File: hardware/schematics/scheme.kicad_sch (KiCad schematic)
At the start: 10 parts

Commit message: changed schema
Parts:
- added CD1: Data Connector, symbol Connector:Conn_01x02_Pin
- added CW1: Power Connector, symbol Connector:Conn_01x02_Pin
- added MOSFET: IRLZ44N, Package_TO_SOT_THT:TO-220-3_Vertical, symbol Transistor_FET:IRLZ44N
- renumbered C1 to D1
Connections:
- net at CP1.3 (Pin_3): now also MOSFET.2 (D)
- net at STEP.1 (SW): no longer A1.17 (RAW)
- net at D1.1 (RO): now also A1.2 (RX1)
- net at D1.2 (~{RE}): now also A1.5 (D2), D1.3 (DE)
- net at D1.4 (DI): now also A1.1 (TX0)
- net at D1.5 (GND): now also A1.29 (GND), A1.4 (GND), CS1.3 (Pin_3), CW1.2 (Pin_2), MOSFET.3 (S)
- net at D1.6 (A): now also CD1.1 (Pin_1); no longer C0.6 (A)
- net at D1.7 (B): now also CD1.2 (Pin_2); no longer C0.7 (B)
- net at D1.8 (VCC): now also A1.17 (RAW), CS1.1 (Pin_1), CW1.1 (Pin_1)
- net at CS1.2 (Pin_2): now also A1.19 (A0)
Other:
- moved on the sheet: A1, CP1, CS1, D1

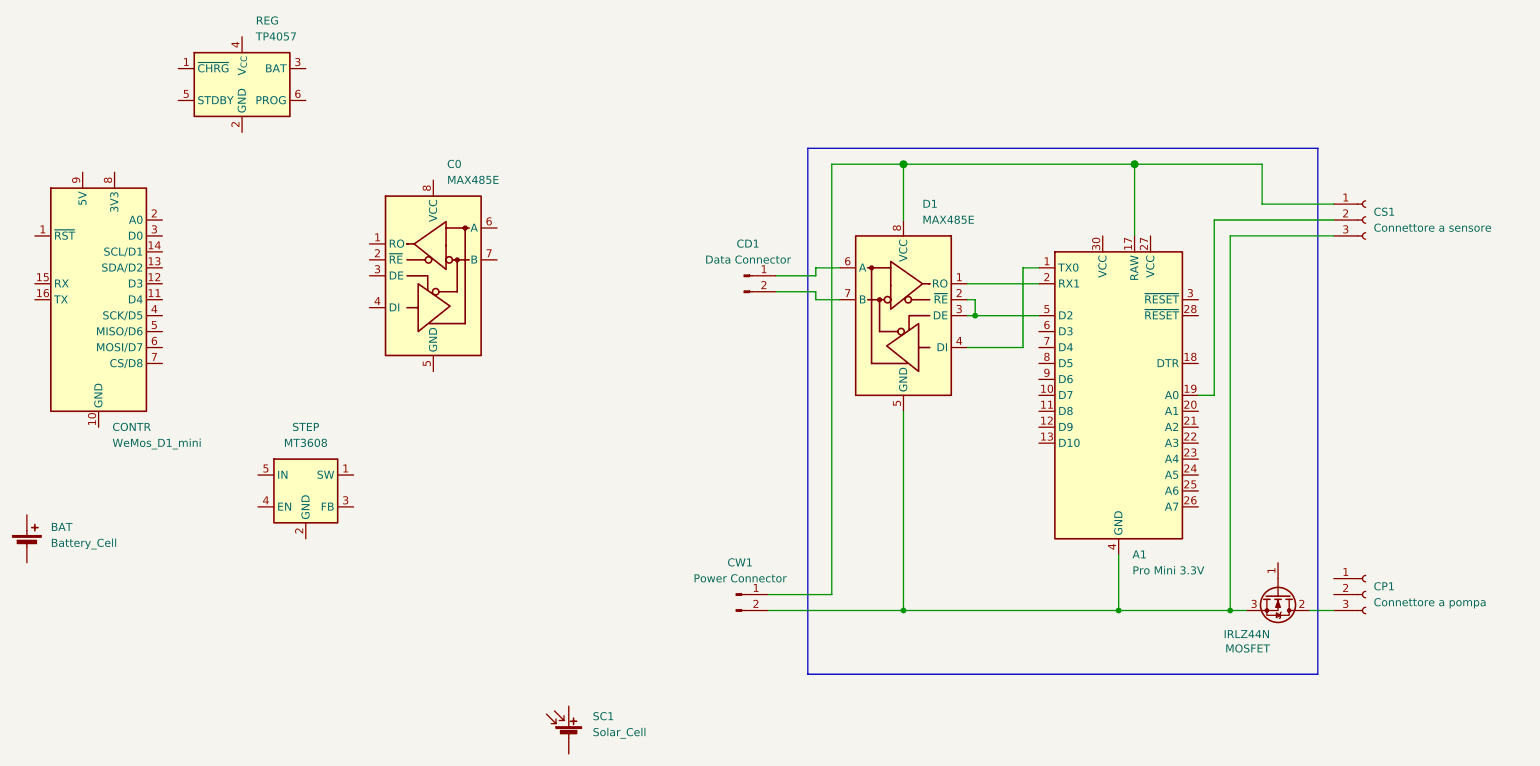
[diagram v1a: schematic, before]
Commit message: plant client schema almost complete
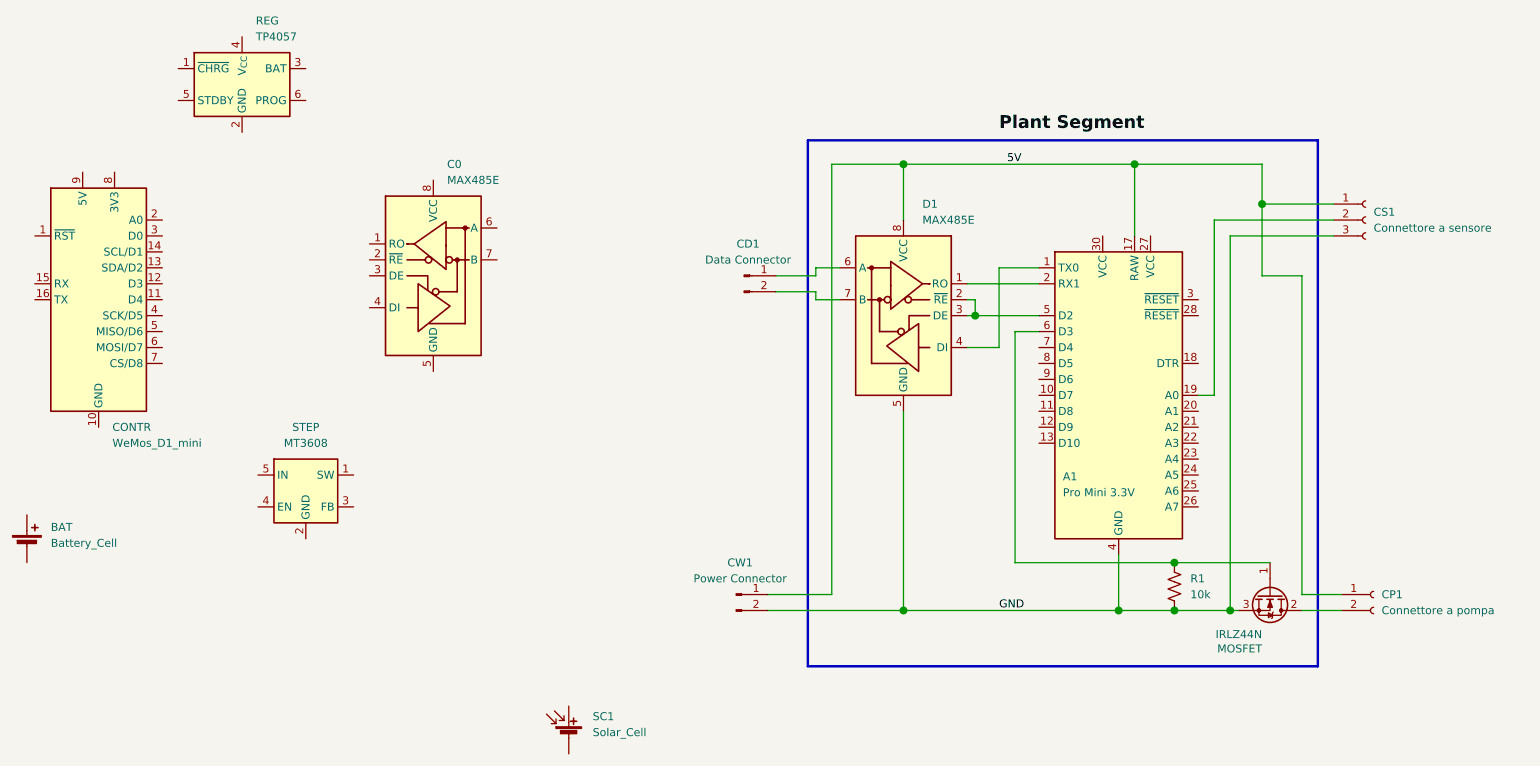
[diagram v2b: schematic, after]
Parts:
- removed CP1: Connettore a pompa, symbol Connector:Conn_01x03_Socket
- added CP1: Connettore a pompa, symbol Connector:Conn_01x02_Socket
- added R1: 10k, symbol Device:R_US
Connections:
- net at MOSFET.2 (D): now also CP1.2 (Pin_2)
- net GND: now reaches A1.29 (GND), A1.4 (GND), CS1.3 (Pin_3), CW1.2 (Pin_2), D1.5 (GND), MOSFET.3 (S)
- net GND: now also R1.2
- net 5V: now reaches A1.17 (RAW), CS1.1 (Pin_1), CW1.1 (Pin_1), D1.8 (VCC)
- net 5V: now also CP1.1 (Pin_1)
- net at MOSFET.1 (G): now also A1.6 (D3), R1.1
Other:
- moved on the sheet: MOSFET
